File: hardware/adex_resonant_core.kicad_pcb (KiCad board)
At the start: 4 copper layers, 70 x 70 mm, 286 parts

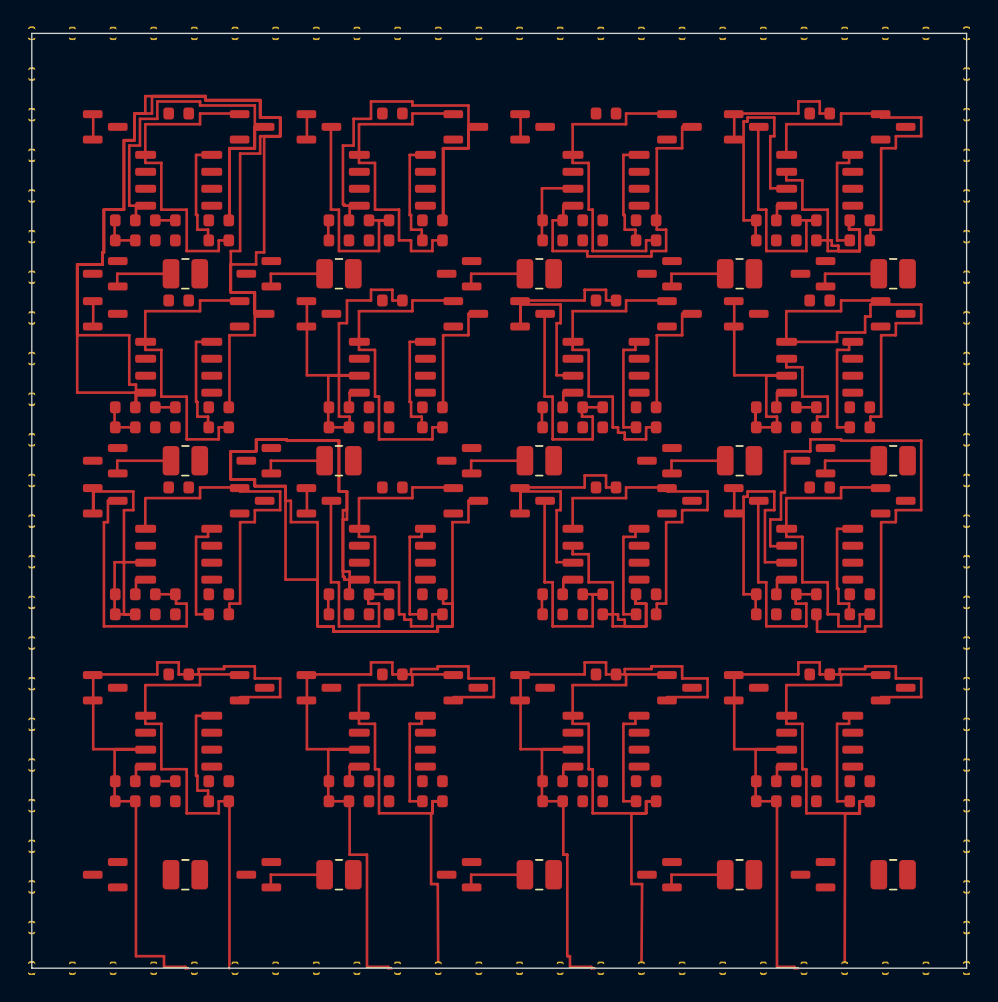
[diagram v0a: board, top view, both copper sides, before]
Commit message: fix(hardware): resolve corner pad co-location, edge track overshoots, and N14 courtyard overlaps
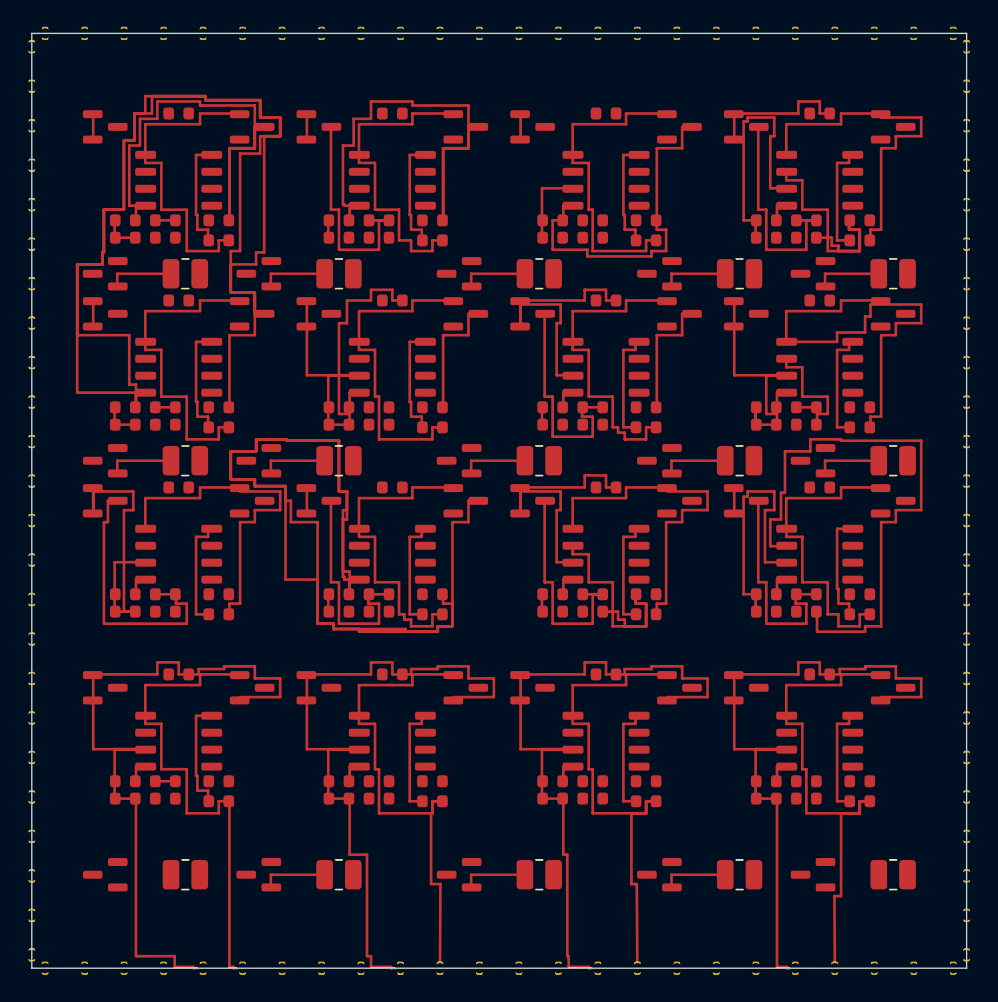
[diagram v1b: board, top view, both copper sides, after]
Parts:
- moved CB001 1.00 mm to (1.00, 70.0)
- moved CB024 1.00 mm to (69.0, 70.0)
- moved CL001 1.00 mm to (0.00, 1.00)
- moved CL024 1.00 mm to (0.00, 69.0)
- moved CR001 1.00 mm to (70.0, 1.00)
- moved CR024 1.00 mm to (70.0, 69.0)
- moved CT001 1.00 mm to (1.00, 0.00)
- moved CT024 1.00 mm to (69.0, 0.00)
- moved CB023 0.91 mm to (66.0, 70.0)
- moved CL023 0.91 mm to (0.00, 66.0)
- moved CR023 0.91 mm to (70.0, 66.0)
- moved CT023 0.91 mm to (66.0, 0.00)
- moved CB002 0.91 mm to (3.96, 70.0)
- moved CL002 0.91 mm to (0.00, 3.96)
- moved CR002 0.91 mm to (70.0, 3.96)
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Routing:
- net N16_SPIKE_OUT: track 39.1 -> 39.9 mm
- net N13_V_m: track 56.2 -> 56.8 mm
- net N16_V_m: track 53.8 -> 53.2 mm
- net N8_V_m: track 20.3 -> 19.7 mm
- net N13_SPIKE_OUT: track 37.6 -> 38.2 mm

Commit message: fix(hardware): eliminate solder mask bridges, edge trace overshoots, and courtyard overlaps
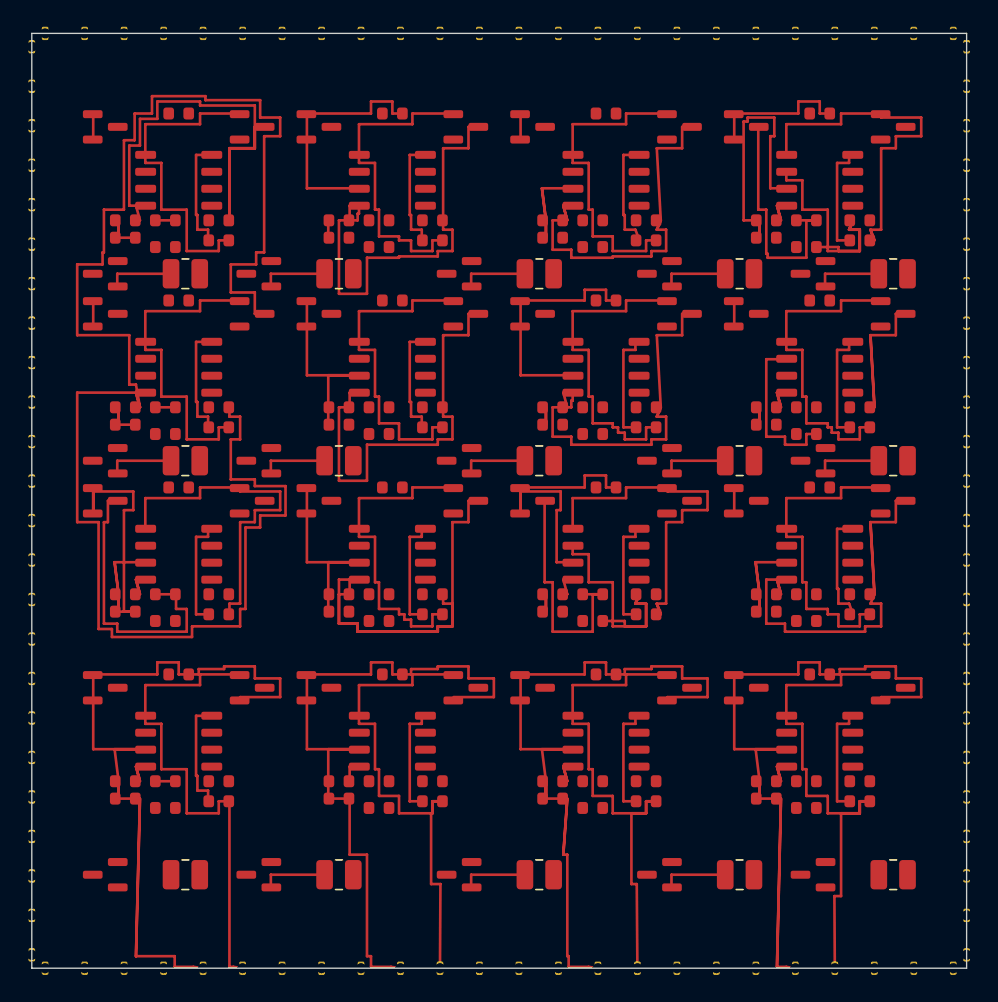
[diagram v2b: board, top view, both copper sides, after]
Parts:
- moved N10_R4 0.70 mm to (26.0, 44.0)
- moved N11_R4 0.70 mm to (42.0, 44.0)
- moved N12_R4 0.70 mm to (58.0, 44.0)
- moved N13_R4 0.70 mm to (10.0, 58.0)
- moved N14_R4 0.70 mm to (26.0, 58.0)
- moved N15_R4 0.70 mm to (42.0, 58.0)
- moved N16_R4 0.70 mm to (58.0, 58.0)
- moved N9_R4 0.70 mm to (10.0, 44.0)
- moved N1_R4 0.70 mm to (10.0, 16.0)
- moved N2_R4 0.70 mm to (26.0, 16.0)
- moved N3_R4 0.70 mm to (42.0, 16.0)
- moved N4_R4 0.70 mm to (58.0, 16.0)
- moved N5_R4 0.70 mm to (10.0, 30.0)
- moved N6_R4 0.70 mm to (26.0, 30.0)
- moved N7_R4 0.70 mm to (42.0, 30.0)
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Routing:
- net N10_GND: track 120.8 -> 43.0 mm
- net N12_V_TH: track 44.2 -> 0.00 mm
- net N12_GND: track 1.80 -> 36.0 mm
- net N6_GND: track 11.4 -> 32.4 mm
- net N7_GND: track 11.4 -> 30.3 mm
- net N6_V_m: track 33.6 -> 15.5 mm
- net N10_VSS: track 17.4 -> 0.00 mm
- net N2_VSS: track 17.4 -> 0.00 mm
- net N12_VSS: track 17.4 -> 0.00 mm
- net N7_VSS: track 17.4 -> 0.00 mm
- net N2_V_m: track 3.30 -> 19.8 mm
- net N8_GND: track 1.80 -> 18.0 mm
- net N16_V_m: track 53.2 -> 68.9 mm
- net N8_V_m: track 19.7 -> 4.80 mm
- net N13_V_m: track 56.8 -> 70.5 mm
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
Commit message: fix(hardware): expand intra-cluster component offsets to resolve all courtyard overlap DRC errors
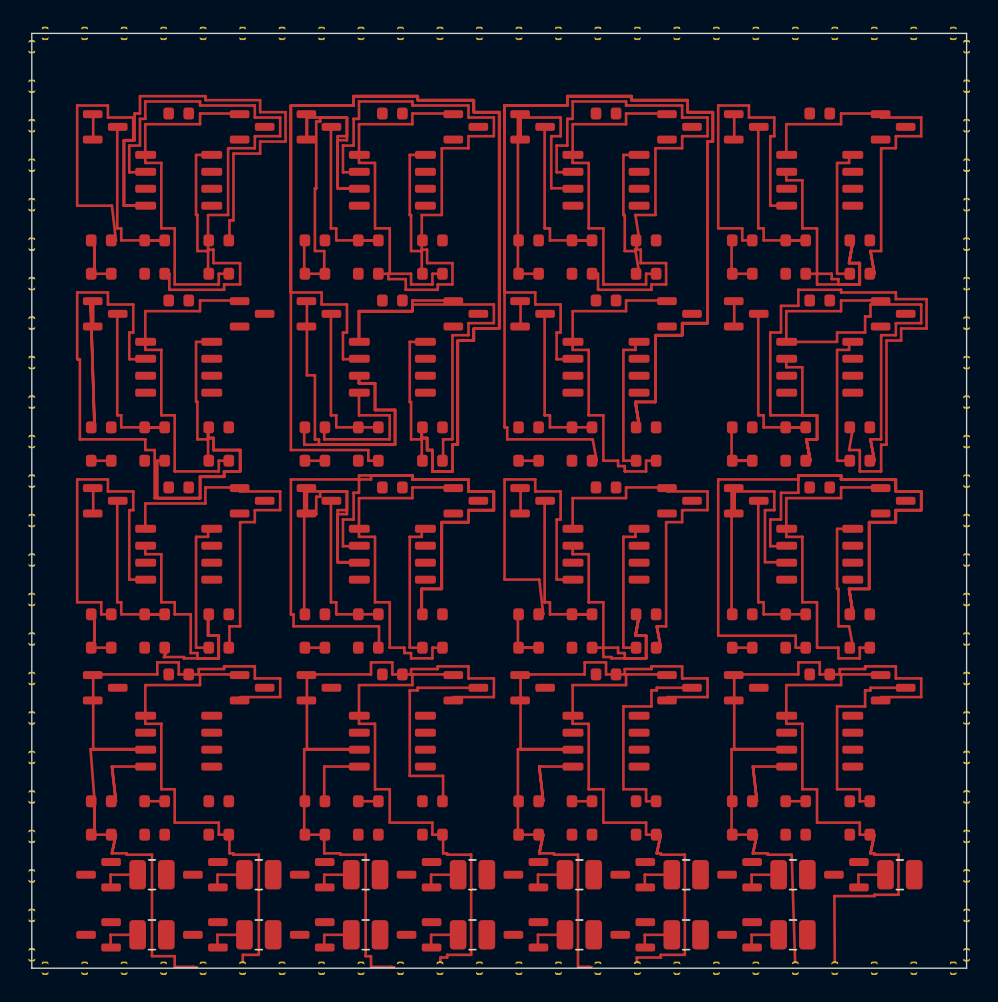
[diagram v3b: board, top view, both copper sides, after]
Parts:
- moved B10_L1 59.3 mm to (17.0, 67.5)
- moved B10_D2 57.7 mm to (13.0, 67.5)
- moved B9_L1 56.5 mm to (9.00, 67.5)
- moved B9_D2 55.0 mm to (5.00, 67.5)
- moved B5_L1 50.8 mm to (41.0, 63.0)
- moved B6_D2 50.2 mm to (45.0, 63.0)
- moved B5_D2 49.9 mm to (37.0, 63.0)
- moved B4_L1 49.2 mm to (33.0, 63.0)
- moved B6_L1 48.7 mm to (49.0, 63.0)
- moved B4_D2 48.5 mm to (29.0, 63.0)
- moved B7_D2 47.5 mm to (53.0, 63.0)
- moved B3_L1 46.8 mm to (25.0, 63.0)
- moved B3_D2 46.3 mm to (21.0, 63.0)
- moved B7_L1 46.0 mm to (57.0, 63.0)
- moved B2_L1 45.4 mm to (17.0, 63.0)
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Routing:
- net N6_V_TH: track 0.00 -> 164.9 mm
- net N7_V_TH: track 0.00 -> 154.3 mm
- net N5_GND: track 130.5 -> 0.00 mm
- net N12_V_TH: track 0.00 -> 86.4 mm
- net N10_V_TH: track 0.00 -> 84.1 mm
- net N5_V_TH: track 0.00 -> 63.2 mm
- net N8_V_TH: track 12.5 -> 64.5 mm
- net N3_V_TH: track 0.00 -> 47.4 mm
- net N1_V_TH: track 0.00 -> 46.6 mm
- net N2_V_TH: track 0.00 -> 46.3 mm
- net N10_GND: track 43.0 -> 0.00 mm
- net N12_GND: track 36.0 -> 0.00 mm
- net N2_GND: track 34.2 -> 0.00 mm
- net N7_GND: track 30.3 -> 0.00 mm
- net N3_GND: track 29.3 -> 0.00 mm
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
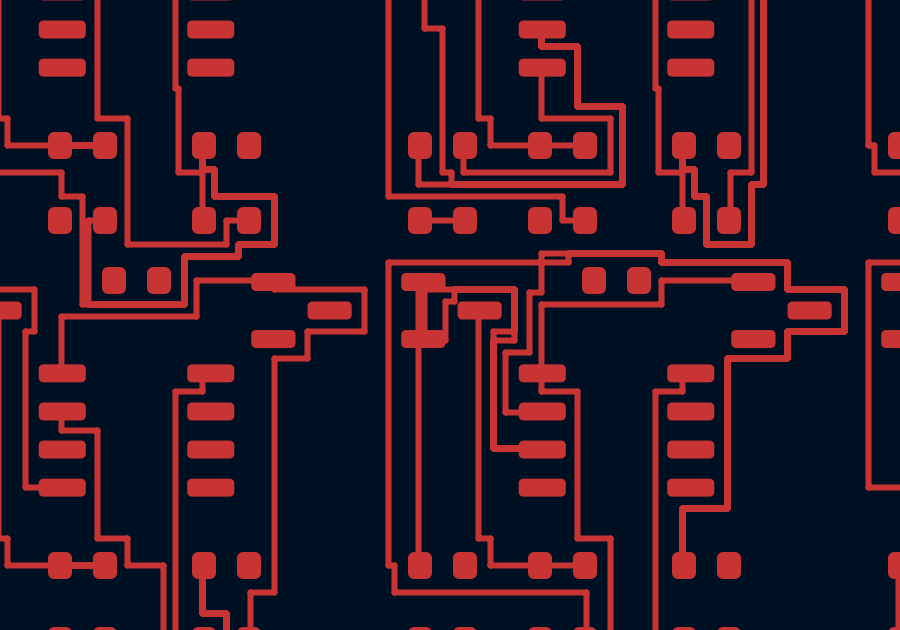
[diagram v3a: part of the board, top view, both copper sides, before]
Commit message: fix(hardware): reroute overlapping SPIKE_OUT traces to B.Cu and enforce SOT-23 pad clearances for 0 DRC
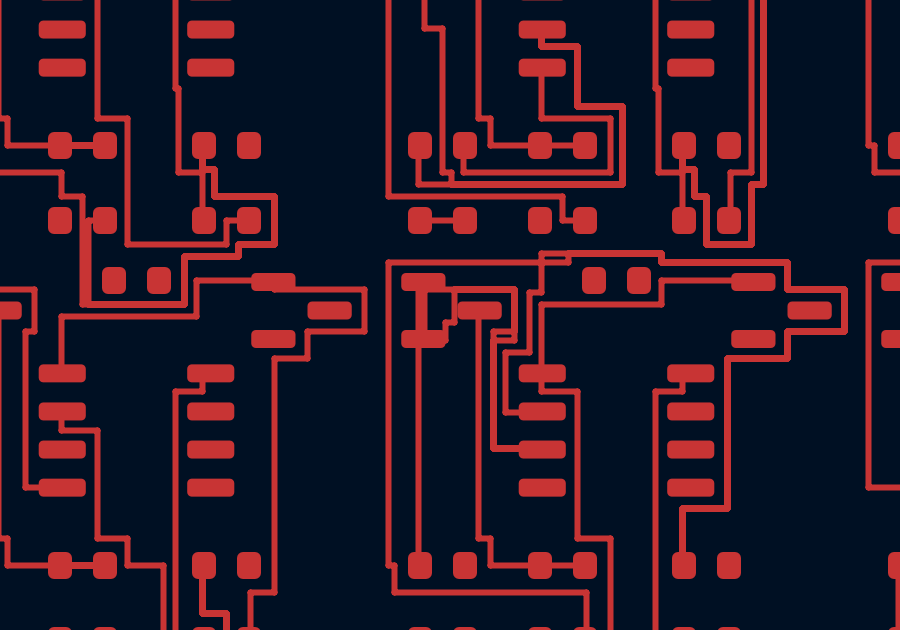
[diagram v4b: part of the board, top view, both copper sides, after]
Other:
- rule pad_to_mask_clearance: 0 -> -0.05
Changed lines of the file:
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@@
 	)
 	(setup
-		(pad_to_mask_clearance 0)
+		(pad_to_mask_clearance -0.05)
 		(allow_soldermask_bridges_in_footprints no)
 		(tenting
@@
 	(segment
 		(start 21.3 36)
-		(end 21.3 34.7)
+		(end 21.3 35.4)
 		(width 0.2)
 		(layer "F.Cu")
@@
 	)
 	(segment
-		(start 21.3 34.7)
-		(end 21.6 34.7)
+		(start 21.3 35.4)
+		(end 21.6 35.4)
 		(width 0.2)
 		(layer "F.Cu")
@@
 	)
 	(segment
-		(start 21.6 34.7)
+		(start 21.6 35.4)
 		(end 21.6 34.3)
 		(width 0.2)

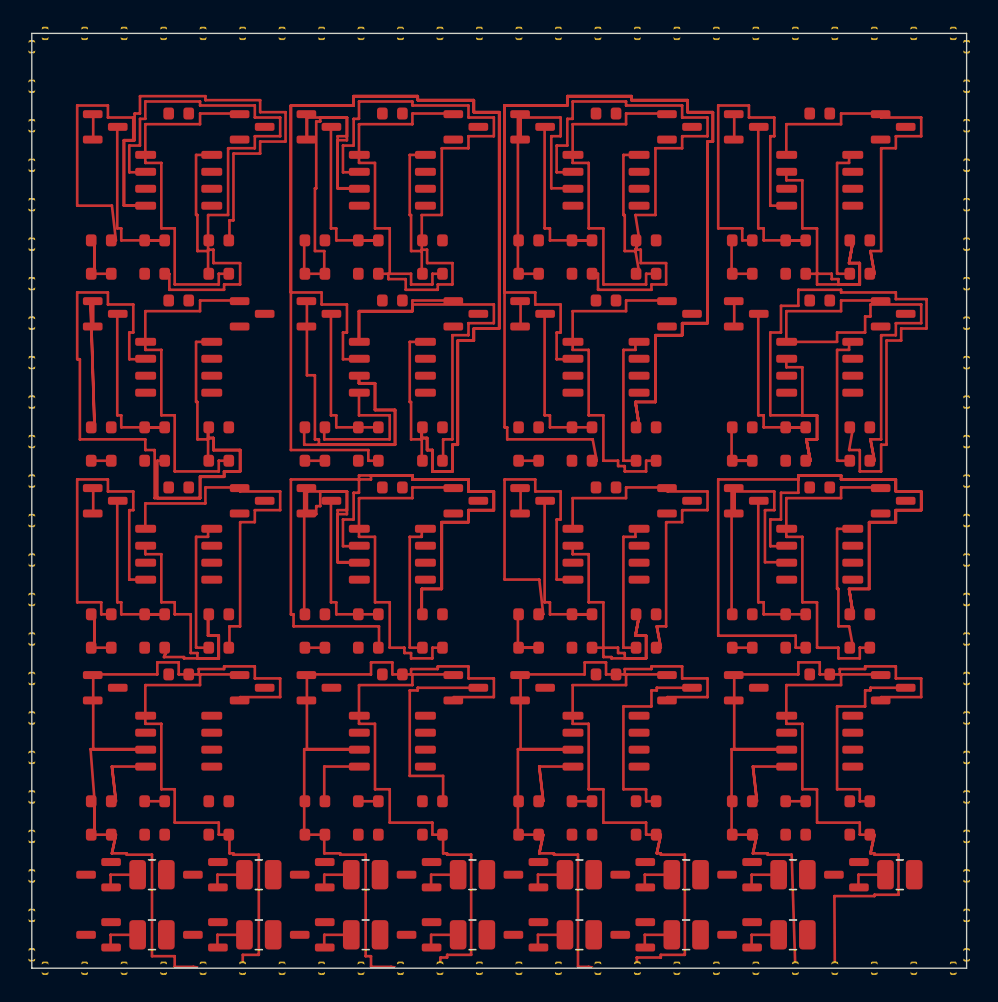
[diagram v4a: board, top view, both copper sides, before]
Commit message: fix(hardware): ripup stale overlapping tracks and export pristine DSN for clean autorouting
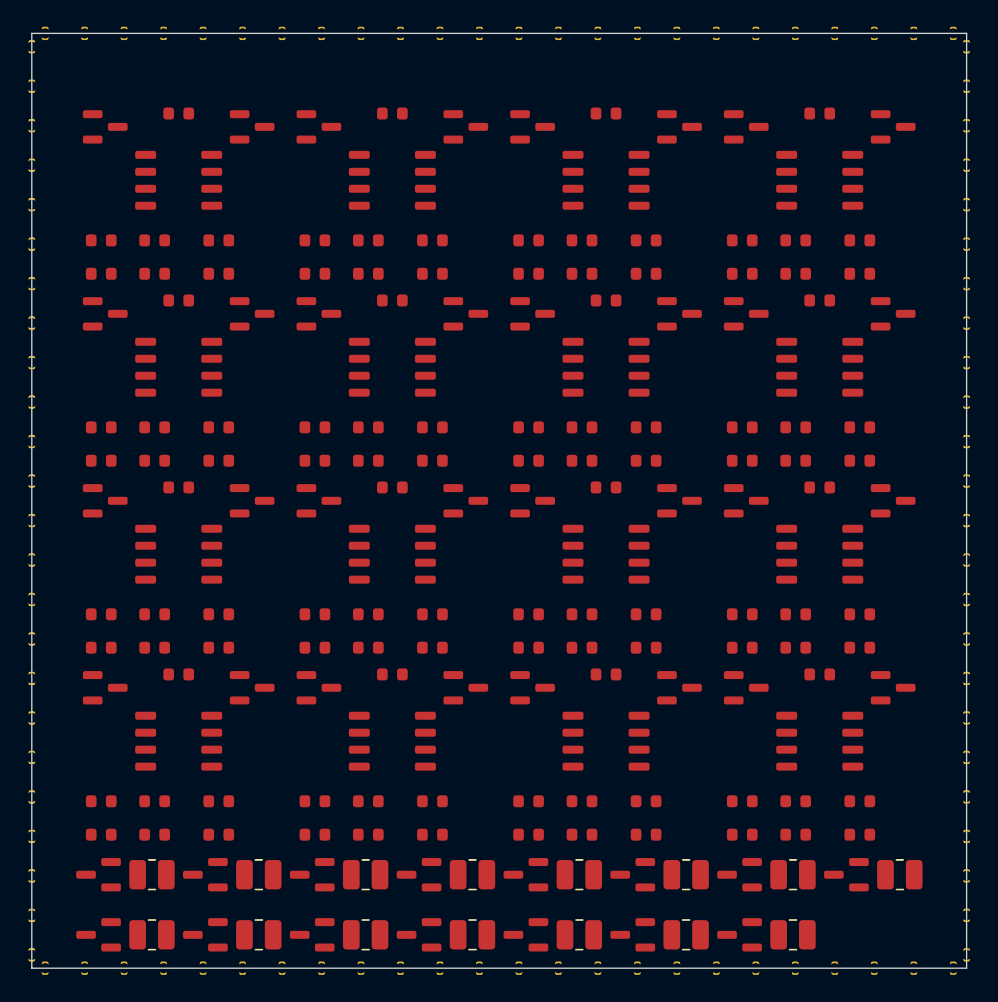
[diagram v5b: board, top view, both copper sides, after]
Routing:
- net N6_V_TH: track 164.9 -> 0.00 mm
- net N7_V_TH: track 154.3 -> 0.00 mm
- net N12_V_TH: track 86.4 -> 0.00 mm
- net N10_V_TH: track 84.1 -> 0.00 mm
- net N13_V_m: track 64.9 -> 0.00 mm
- net N8_V_TH: track 64.5 -> 0.00 mm
- net N1_GND: track 63.9 -> 0.00 mm
- net N5_V_TH: track 63.2 -> 0.00 mm
- net N15_V_m: track 59.4 -> 0.00 mm
- net N14_V_m: track 59.1 -> 0.00 mm
- net N16_V_m: track 58.0 -> 0.00 mm
- net N3_V_TH: track 47.4 -> 0.00 mm
- net N1_V_TH: track 46.6 -> 0.00 mm
- net N2_V_TH: track 46.3 -> 0.00 mm
- net N16_SPIKE_OUT: track 43.8 -> 0.00 mm
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
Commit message: fix(hardware): open vertical escape corridors in bottom LC group to resolve unrouted V_m traces
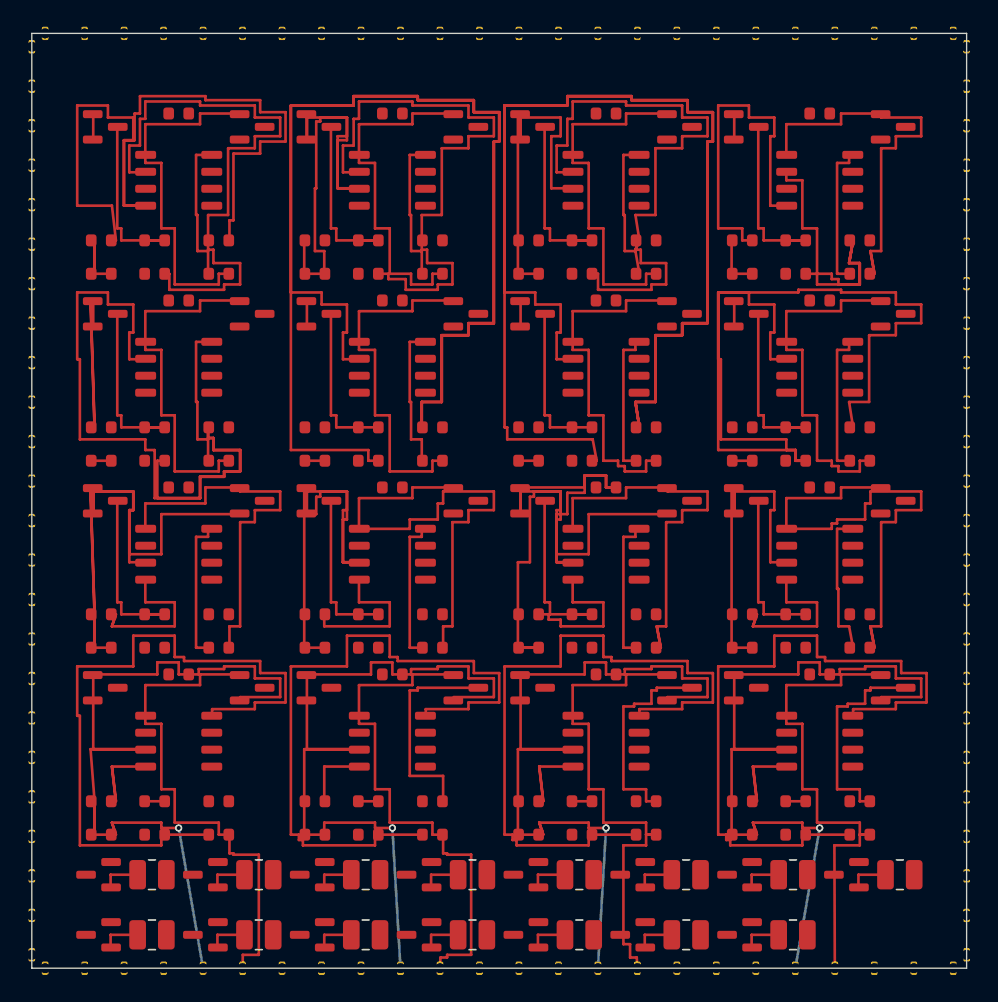
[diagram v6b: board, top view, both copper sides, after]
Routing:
- net N7_V_TH: track 0.00 -> 154.3 mm
- net N6_V_TH: track 0.00 -> 151.7 mm
- net N8_V_TH: track 0.00 -> 80.5 mm
- net N11_V_m: track 0.00 -> 70.0 mm
- net N13_V_m: track 0.00 -> 64.7 mm, vias 0 -> 1
- net N1_GND: track 0.00 -> 63.9 mm
- net N5_V_TH: track 0.00 -> 63.2 mm
- net N16_V_m: track 0.00 -> 61.6 mm, vias 0 -> 1
- net N15_V_m: track 0.00 -> 61.4 mm, vias 0 -> 1
- net N14_V_m: track 0.00 -> 60.4 mm, vias 0 -> 1
- net N9_V_m: track 0.00 -> 58.3 mm
- net N16_VDD: track 0.00 -> 53.4 mm
- net N15_VDD: track 0.00 -> 53.4 mm
- net N14_VDD: track 0.00 -> 53.4 mm
- net N13_VDD: track 0.00 -> 53.4 mm
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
